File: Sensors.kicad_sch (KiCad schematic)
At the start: 15 parts, among them U15 TPRT9013-33, U16 ICM-42688-P, U17 INA230, U18 BMP280

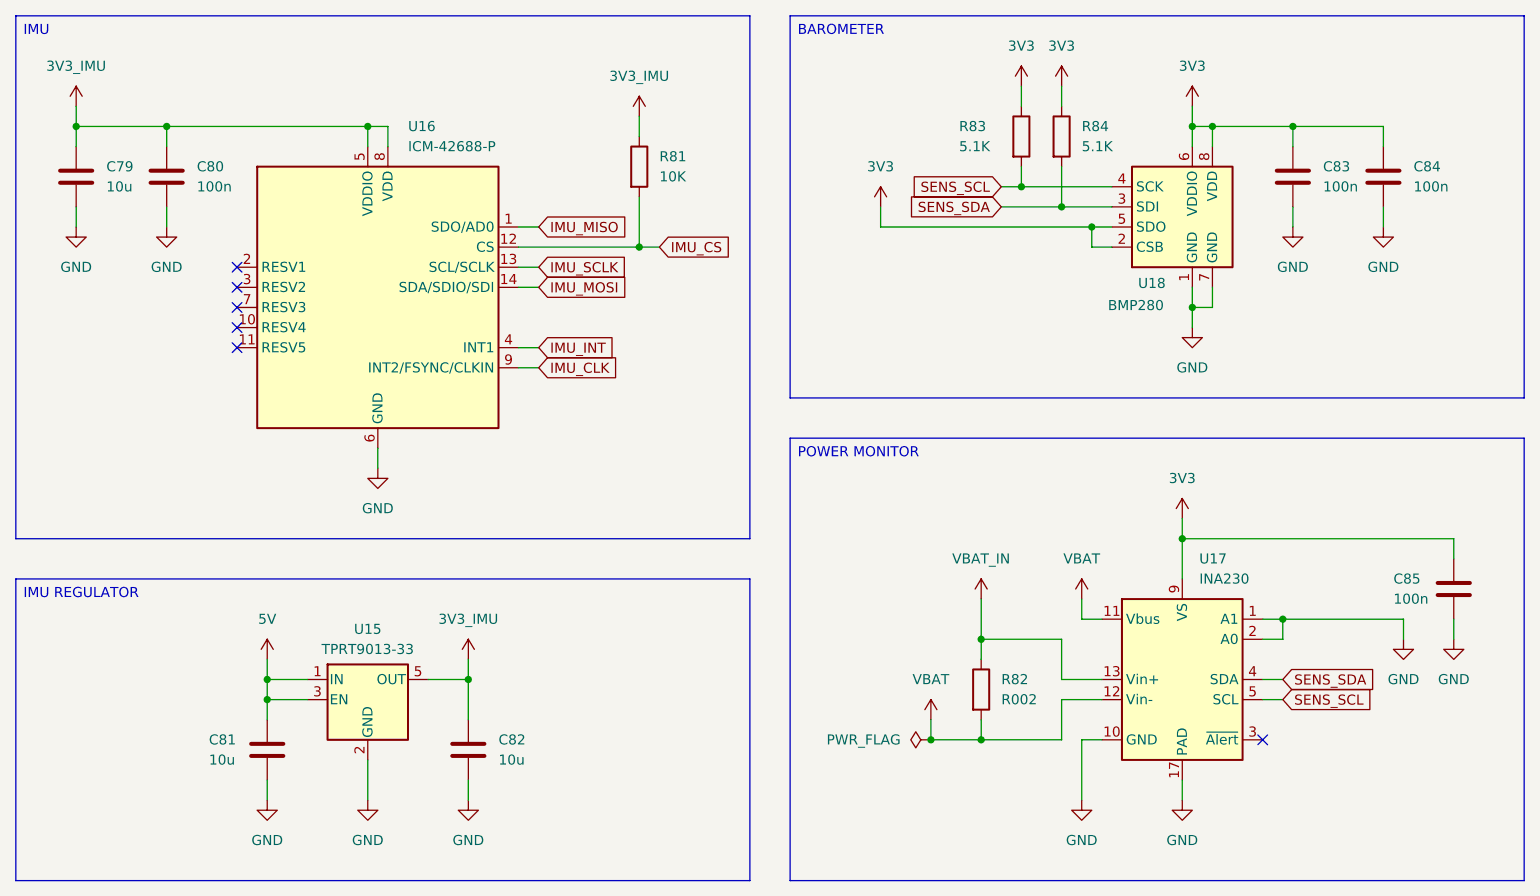
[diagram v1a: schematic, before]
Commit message: IMU filtering and layout
Added a missing capacitor for the IMU.
Updated the PCB layout.
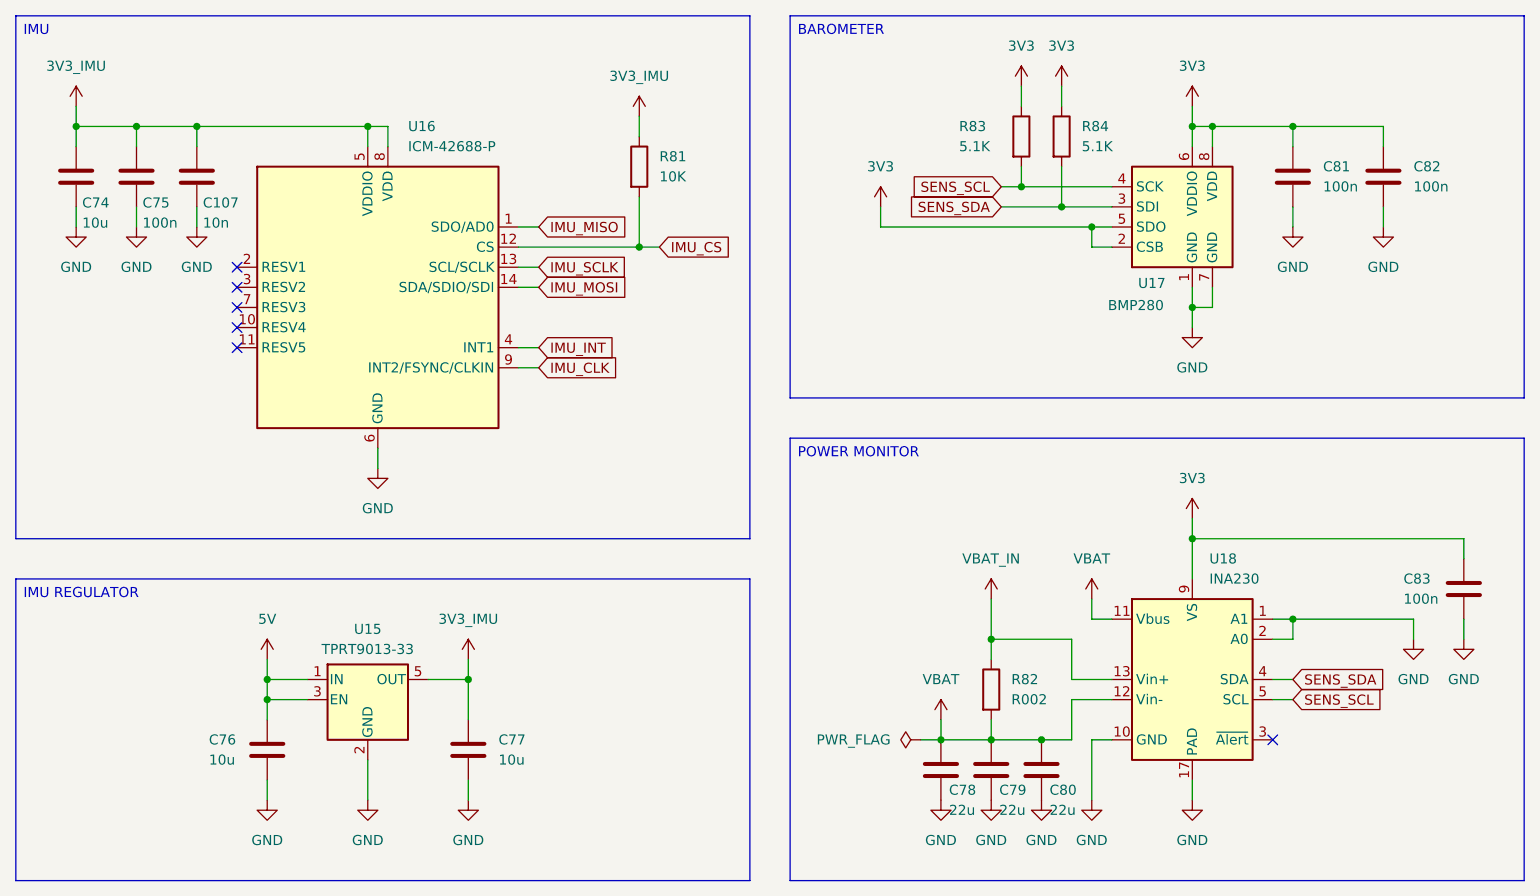
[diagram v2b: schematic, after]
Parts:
- added C107: 10n, Capacitor_SMD:C_0603_1608Metric, symbol Device:C
- added C78, C79, C80: 22u, Capacitor_SMD:C_1206_3216Metric, symbol Device:C
- renumbered C79 to C74, C80 to C75, C81 to C76, C82 to C77, C83 to C81, C84 to C82, C85 to C83, U18 to U17, U17 to U18
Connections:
- net 3V3_IMU: now also C107.1
- net GND: now also C107.2, C78.2, C79.2, C80.2
- net VBAT: now also C78.1, C79.1, C80.1
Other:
- moved on the sheet: C75, C83, R82, U18

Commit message: Oscillator and IMU layout
Updated the oscillator layout for the RP2350.
Updated the IMU layout for the IMU.
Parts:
- renumbered C74 to C75, C75 to C76, C107 to C77, C76 to C78, C77 to C79, C78 to C80, C79 to C81, C80 to C82, C81 to C83, C82 to C84, C83 to C85

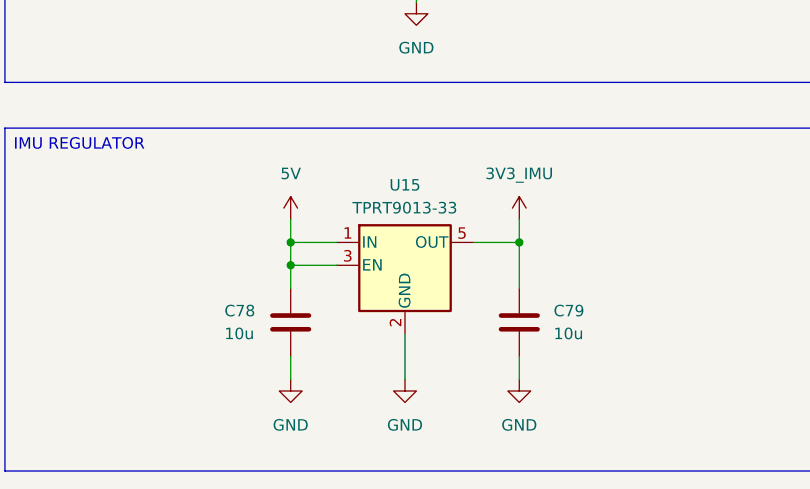
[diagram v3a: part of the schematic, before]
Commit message: Power layout and regulators
Changed the LDO regulators to TLV767.
Added missing power connections.

TODO:
Start the ELRS module layout.
Review previous iterations.
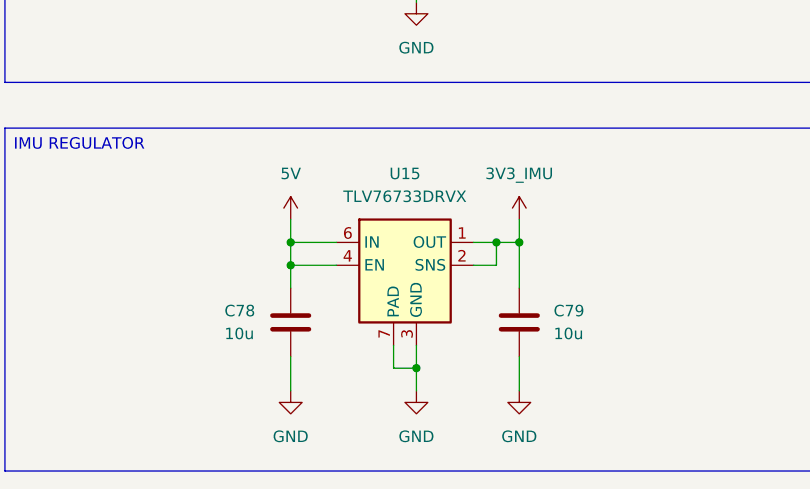
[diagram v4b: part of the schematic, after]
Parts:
- removed U15: TPRT9013-33, Package_TO_SOT_SMD:SOT-23-5, symbol Regulator_Linear:TLV70233_SOT23-5
- added U15: TLV76733DRVX, Package_SON:WSON-6-1EP_2x2mm_P0.65mm_EP1x1.6mm_ThermalVias, symbol Custom_Parts:TLV76733DRVX
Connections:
- net 3V3_IMU: now also U15.1 (OUT), U15.2 (SNS)
- net 5V: now also U15.4 (EN), U15.6 (IN)
- net GND: now also U15.3 (GND), U15.5 (GND), U15.7 (PAD)

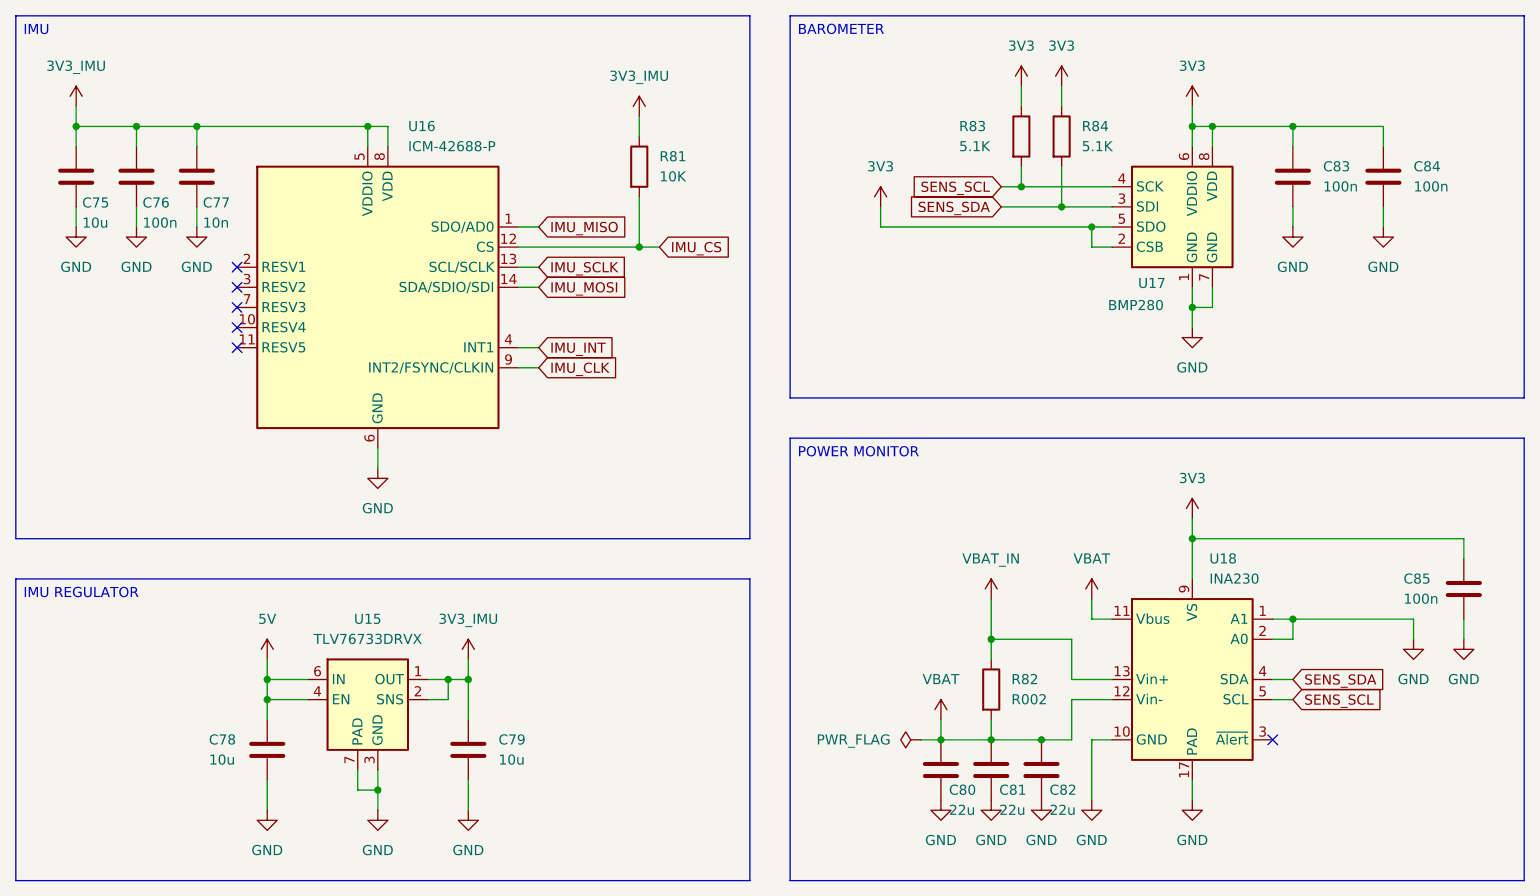
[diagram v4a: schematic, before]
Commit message: Voltage detection
Added a VBUS voltage detection for the RP.
Minor layout changes.
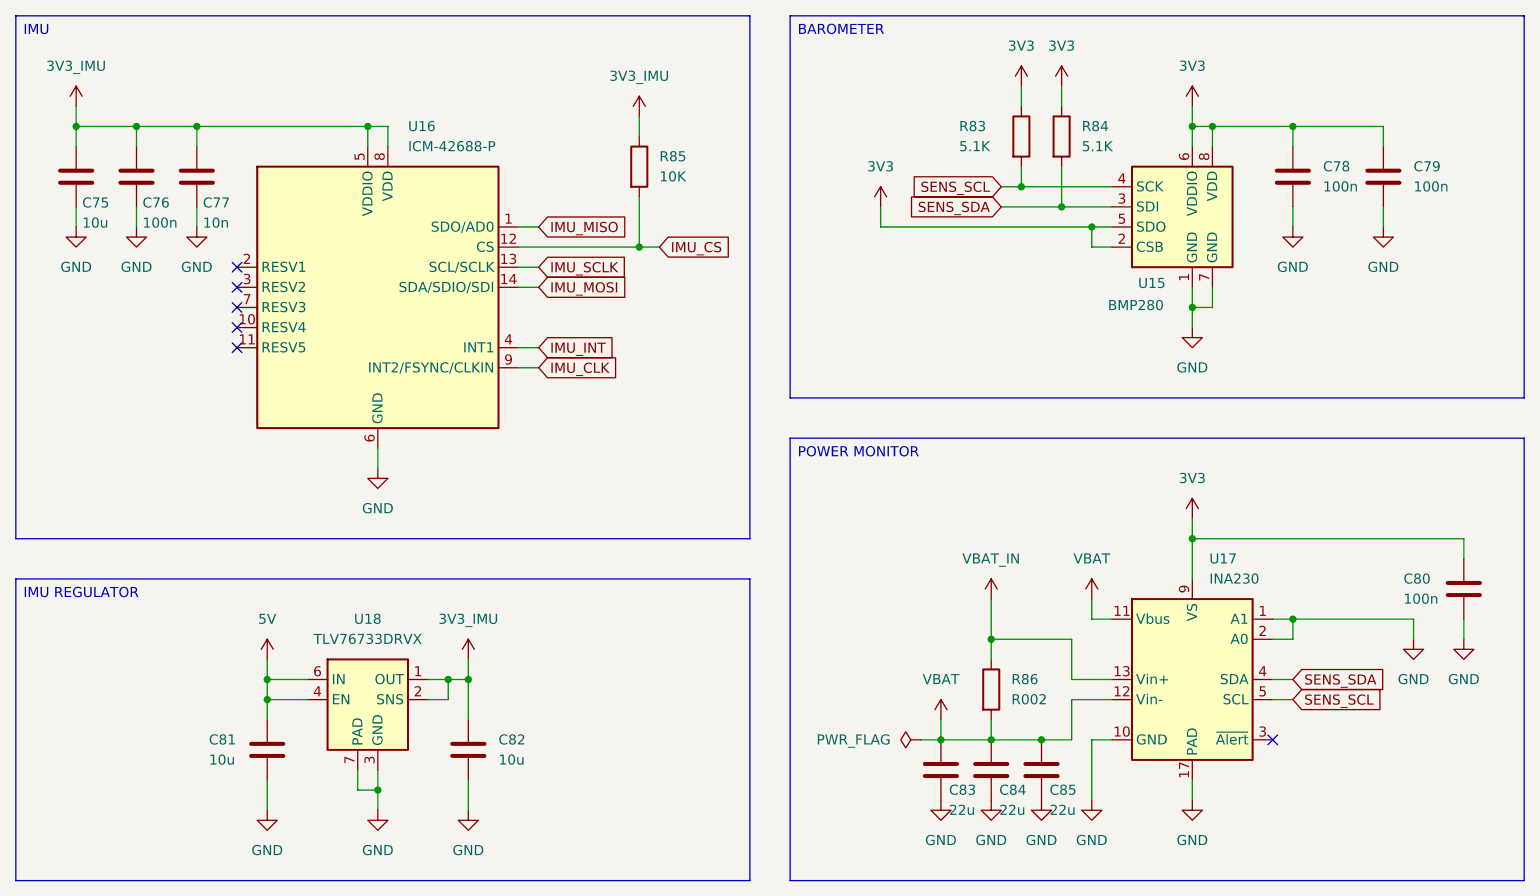
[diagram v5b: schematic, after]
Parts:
- renumbered C83 to C78, C84 to C79, C85 to C80, C78 to C81, C79 to C82, C80 to C83, C81 to C84, C82 to C85, R81 to R85, R82 to R86, U17 to U15, U18 to U17, U15 to U18
